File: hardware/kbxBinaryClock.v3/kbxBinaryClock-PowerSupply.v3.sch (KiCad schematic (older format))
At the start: 8 parts, among them J2 Jack-DC, U5 LD1117S33TR

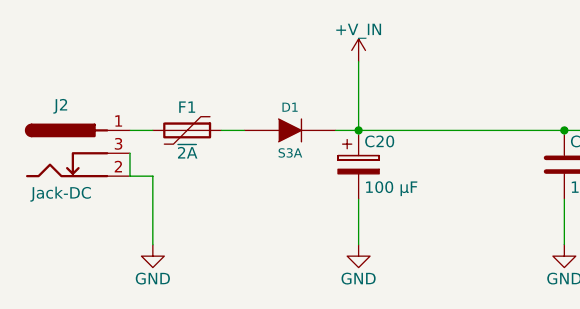
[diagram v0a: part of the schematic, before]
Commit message: Added BoM, hw README, PCB tweaks
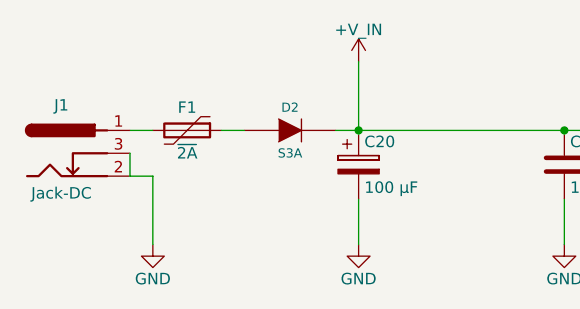
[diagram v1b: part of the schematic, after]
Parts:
- BT1: Part Number (none) -> 103
- C20: Part Number (none) -> 25SVF100M
- D2: renamed from D1; Part Number (none) -> S3A
- F1: Part Number (none) -> 2920L185DR
- U5: Part Number (none) -> LD1117ADT33TR
- renumbered J2 to J1
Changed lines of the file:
@@
 $EndDescr
 $Comp
-L Jack-DC J2
+L Jack-DC J1
 U 1 1 5A06C211
 P 2900 4000
-F 0 "J2" H 2900 4210 50  0000 C CNN
+F 0 "J1" H 2900 4210 50  0000 C CNN
 F 1 "Jack-DC" H 2900 3825 50  0000 C CNN
 F 2 "kbxCustoms:BARREL_JACK" H 2950 3960 50  0001 C CNN
@@
 F 1 "CR2032" H 8300 4000 50  0000 L CNN
 F 2 "Battery_Holders:Keystone_103_1x20mm-CoinCell" V 8200 4060 50  0001 C CNN
-F 3 "" V 8200 4060 50  0001 C CNN
+F 3 "http://www.keyelco.com/product.cfm/product_id/719" V 8200 4060 50  0001 C CNN
+F 4 "103" H 8200 4000 60  0001 C CNN "Part Number"
 	1    8200 4000
 	1    0    0    -1
@@
 F 1 "100 µF" H 4225 3950 50  0000 L CNN
 F 2 "Capacitors_SMD:CP_Elec_8x10" H 4238 3900 50  0001 C CNN
-F 3 "" H 4200 4050 50  0001 C CNN
+F 3 "https://industrial.panasonic.com/ww/products/capacitors/polymer-capacitors/os-con/svf/25SVF100M" H 4200 4050 50  0001 C CNN
+F 4 "25SVF100M" H 4200 4050 60  0001 C CNN "Part Number"
 	1    4200 4050
 	1    0    0    -1
@@
 F 1 "~2A" V 3550 3900 50  0000 C CNN
 F 2 "Fuse_Holders_and_Fuses:Fuse_SMD2920" H 3500 3700 50  0001 L CNN
-F 3 "" H 3450 3900 50  0001 C CNN
+F 3 "http://m.littelfuse.com/~/media/electronics/datasheets/resettable_ptcs/littelfuse_ptc_2920l_datasheet.pdf.pdf" H 3450 3900 50  0001 C CNN
+F 4 "2920L185DR" V 3450 3900 60  0001 C CNN "Part Number"
 	1    3450 3900
 	0    1    1    0
 $EndComp
 $Comp
-L DIODE D1
+L DIODE D2
 U 1 1 5A0B6C19
 P 3900 3900
-F 0 "D1" H 3900 4000 40  0000 C CNN
+F 0 "D2" H 3900 4000 40  0000 C CNN
 F 1 "S3A" H 3900 3800 40  0000 C CNN
 F 2 "Diodes_SMD:D_SMC" H 3900 3900 60  0001 C CNN
-F 3 "" H 3900 3900 60  0000 C CNN
+F 3 "http://www.onsemi.com/pub/Collateral/S3N-D.PDF" H 3900 3900 60  0001 C CNN
+F 4 "S3A" H 3900 3900 60  0001 C CNN "Part Number"
 	1    3900 3900
 	1    0    0    -1
@@
 F 1 "LD1117S33TR" H 5600 4025 50  0000 L CNN
 F 2 "TO_SOT_Packages_SMD:TO-252-2" H 5600 4100 50  0001 C CNN
-F 3 "" H 5700 3650 50  0001 C CNN
+F 3 "http://www.st.com/content/ccc/resource/technical/document/datasheet/a5/c3/3f/c9/2b/15/40/49/CD00002116.pdf/files/CD00002116.pdf/jcr:content/translations/en.CD00002116.pdf" H 5700 3650 50  0001 C CNN
+F 4 "LD1117ADT33TR" H 5600 3900 60  0001 C CNN "Part Number"
 	1    5600 3900
 	1    0    0    -1

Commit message: Updated for KiCad v5, updated silks
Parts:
- BT1: symbol Battery_Cell -> kbxBinaryClock.v3-rescue:Battery_Cell
- C20: symbol CP -> kbxBinaryClock.v3-rescue:CP
- C21, C22: symbol C -> kbxBinaryClock.v3-rescue:C
- D2: symbol DIODE -> kbxBinaryClock.v3-rescue:DIODE
- F1: symbol Polyfuse -> kbxBinaryClock.v3-rescue:Polyfuse
- J1: symbol Jack-DC -> kbxBinaryClock.v3-rescue:Jack-DC
- U5: symbol LD1117S33TR_SOT223 -> kbxBinaryClock.v3-rescue:LD1117S33TR_SOT223
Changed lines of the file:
@@
-EESchema Schematic File Version 2
-LIBS:power
-LIBS:device
-LIBS:transistors
-LIBS:conn
-LIBS:linear
-LIBS:regul
-LIBS:74xx
-LIBS:cmos4000
-LIBS:adc-dac
-LIBS:memory
-LIBS:xilinx
-LIBS:microcontrollers
-LIBS:dsp
-LIBS:microchip
-LIBS:analog_switches
-LIBS:motorola
-LIBS:texas
-LIBS:intel
-LIBS:audio
-LIBS:interface
-LIBS:digital-audio
-LIBS:philips
-LIBS:display
-LIBS:cypress
-LIBS:siliconi
-LIBS:opto
-LIBS:atmel
-LIBS:contrib
-LIBS:valves
-LIBS:stm32
-LIBS:win
-LIBS:mechanical
-LIBS:switches
-LIBS:maxim
-LIBS:sensors
+EESchema Schematic File Version 4
 LIBS:kbxBinaryClock.v3-cache
-EELAYER 25 0
+EELAYER 26 0
 EELAYER END
 $Descr A4 11693 8268
@@
 $EndDescr
 $Comp
-L Jack-DC J1
+L kbxBinaryClock.v3-rescue:Jack-DC J1
 U 1 1 5A06C211
 P 2900 4000
@@
 $EndComp
 $Comp
-L C C22
+L kbxBinaryClock.v3-rescue:C C22
 U 1 1 5A06C24E
 P 6100 4050
@@
 $EndComp
 $Comp
-L C C21
+L kbxBinaryClock.v3-rescue:C C21
 U 1 1 5A06C283
 P 5100 4050
@@
 $EndComp
 $Comp
-L Battery_Cell BT1
+L kbxBinaryClock.v3-rescue:Battery_Cell BT1
 U 1 1 5A06C2CC
 P 8200 4000
@@
 $EndComp
 $Comp
-L CP C20
+L kbxBinaryClock.v3-rescue:CP C20
 U 1 1 5A0AB81C
 P 4200 4050
@@
 $EndComp
 $Comp
-L +BATT #PWR027
+L kbxBinaryClock.v3-rescue:+BATT #PWR027
 U 1 1 5A0AB8E2
 P 8200 3600
@@
 $EndComp
 $Comp
-L +3.3V #PWR028
+L kbxBinaryClock.v3-rescue:+3.3V #PWR028
 U 1 1 5A0AB93A
 P 6600 3600
@@
 $EndComp
 $Comp
-L GND #PWR029
+L kbxBinaryClock.v3-rescue:GND #PWR029
 U 1 1 5A0ABA04
 P 4200 4400
@@
 $EndComp
 $Comp
-L GND #PWR030
+L kbxBinaryClock.v3-rescue:GND #PWR030
 U 1 1 5A0ABA30
 P 5100 4400
@@
 $EndComp
 $Comp
-L GND #PWR031
+L kbxBinaryClock.v3-rescue:GND #PWR031
 U 1 1 5A0ABA5C
 P 5600 4400
@@
 $EndComp
 $Comp
-L GND #PWR032
+L kbxBinaryClock.v3-rescue:GND #PWR032
 U 1 1 5A0ABA88
 P 6100 4400
@@
 $EndComp
 $Comp
-L GND #PWR033
+L kbxBinaryClock.v3-rescue:GND #PWR033
 U 1 1 5A0ABAB4
 P 8200 4400
@@
 $EndComp
 $Comp
-L Polyfuse F1
+L kbxBinaryClock.v3-rescue:Polyfuse F1
 U 1 1 5A0B6BAC
 P 3450 3900
@@
 $EndComp
 $Comp
-L DIODE D2
+L kbxBinaryClock.v3-rescue:DIODE D2
 U 1 1 5A0B6C19
 P 3900 3900
@@
 $EndComp
 $Comp
-L GND #PWR034
+L kbxBinaryClock.v3-rescue:GND #PWR034
 U 1 1 5A0B6F52
 P 3300 4400
@@
 $EndComp
 $Comp
-L LD1117S33TR_SOT223 U5
+L kbxBinaryClock.v3-rescue:LD1117S33TR_SOT223 U5
 U 1 1 5A06C0AF
 P 5600 3900
@@
 	3200 4000 3200 4100
 $Comp
-L +V_IN #PWR035
+L kbxBinaryClock.v3-rescue:+V_IN #PWR035
 U 1 1 5A7F3BB0
 P 4200 3600
